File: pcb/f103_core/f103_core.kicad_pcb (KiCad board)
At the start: 2 copper layers, 29 parts, among them J1 Conn_02x20_Odd_Even, J4 Conn_01x04, J5 Conn_02x03_Odd_Even, SW1 SW_Push, U1 STM32F103C6Tx, U2 AMS1117-3.3, Y1 8M, Y2 32.768

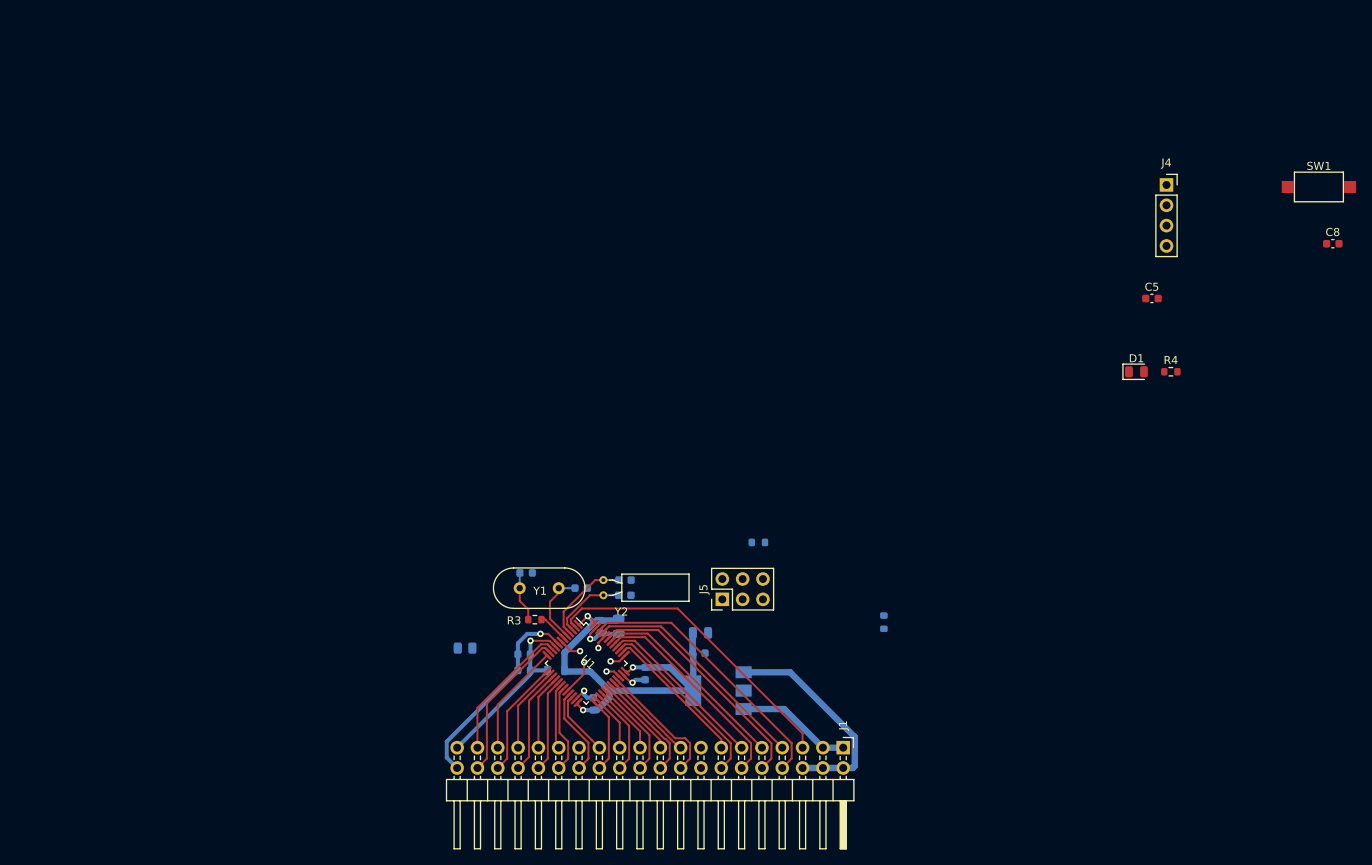
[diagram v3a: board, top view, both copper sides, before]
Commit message: Upadate pcb layout for f103_core board.
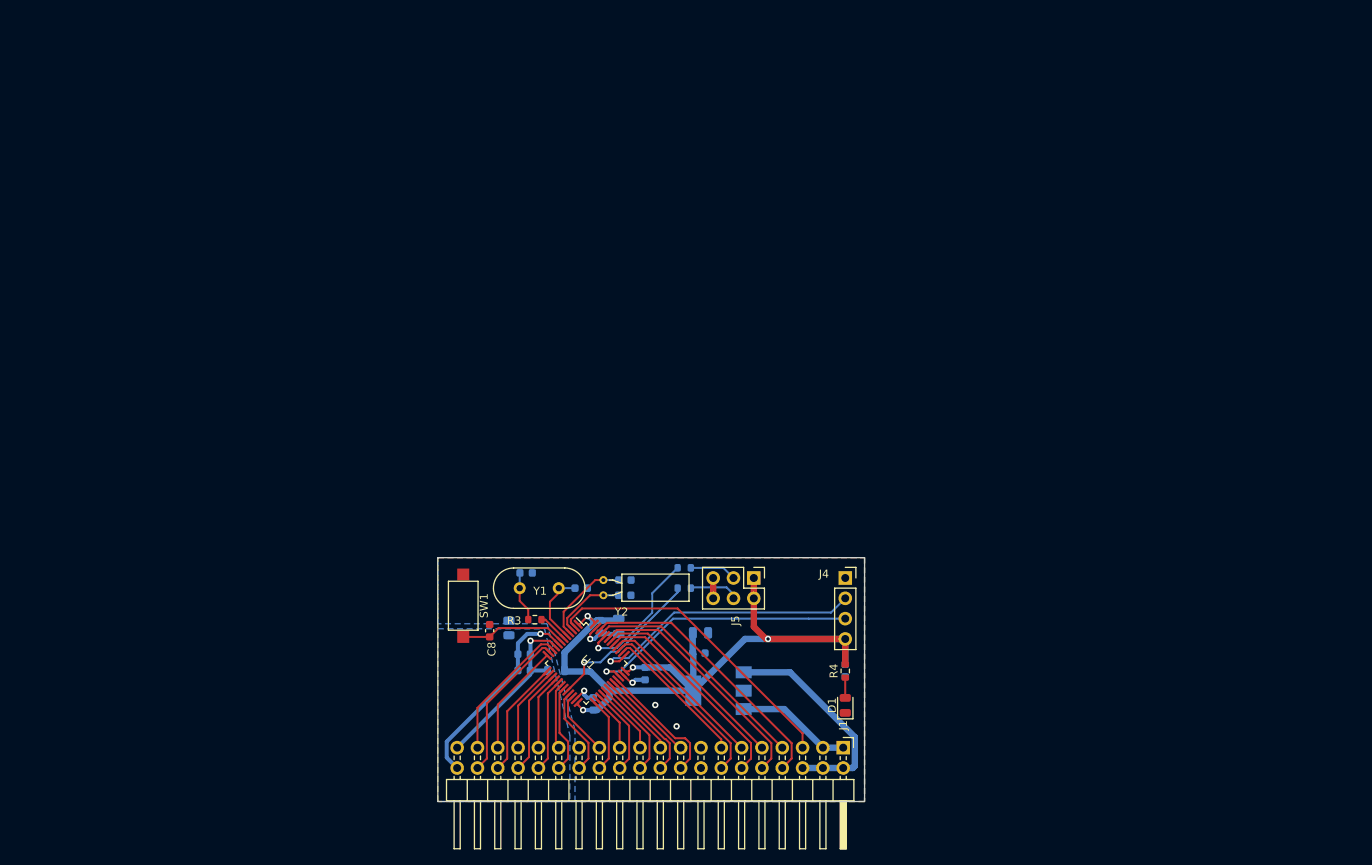
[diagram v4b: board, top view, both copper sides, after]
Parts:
- C5: moved to B.Cu
- moved SW1 119.1 mm to (106.7, 111.4), turned to 270 degrees
- moved C8 116.0 mm to (110.0, 114.5), turned to 90 degrees
- moved J4 63.5 mm to (154.4, 108.0)
- moved C5 60.3 mm to (154.4, 119.5), turned to 270 degrees
- moved D1 55.4 mm to (154.4, 123.9), turned to 90 degrees
- moved R4 55.3 mm to (154.4, 119.6), turned to 90 degrees
- moved R2 25.3 mm to (134.3, 109.2), turned to 0 degrees
- moved R1 9.80 mm to (134.3, 106.7)
- moved R5 6.03 mm to (112.4, 114.2), turned to 270 degrees
- moved J5 4.76 mm to (143.0, 108.0), turned to 270 degrees
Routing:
- net +3V3: track 56.1 -> 102.3 mm, vias 3 -> 4
- net /SYS_JTCK-SWCL: track 2.15 -> 34.7 mm
- net /SYS_JTMS-SWDIO: track 1.93 -> 34.5 mm
- net /BOOT1: track 4.49 -> 20.3 mm
- net /BOOT0: track 1.97 -> 17.5 mm
- net RESET: track 2.87 -> 13.4 mm, vias 1 -> 0
- net Net-(J5-Pad4): track 0.00 -> 6.34 mm
- net Net-(J5-Pad3): track 0.00 -> 5.97 mm
- net Net-(D1-Pad2): track 0.00 -> 2.54 mm
- net GND: track 40.0 -> 42.6 mm, vias 3 -> 5
- added copper zone on B.Cu, net GND
- added copper zone on F.Cu, net GND
- added copper zone on B.Cu, net GNDA
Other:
- board outline added: 53.3 x 30.5 mm

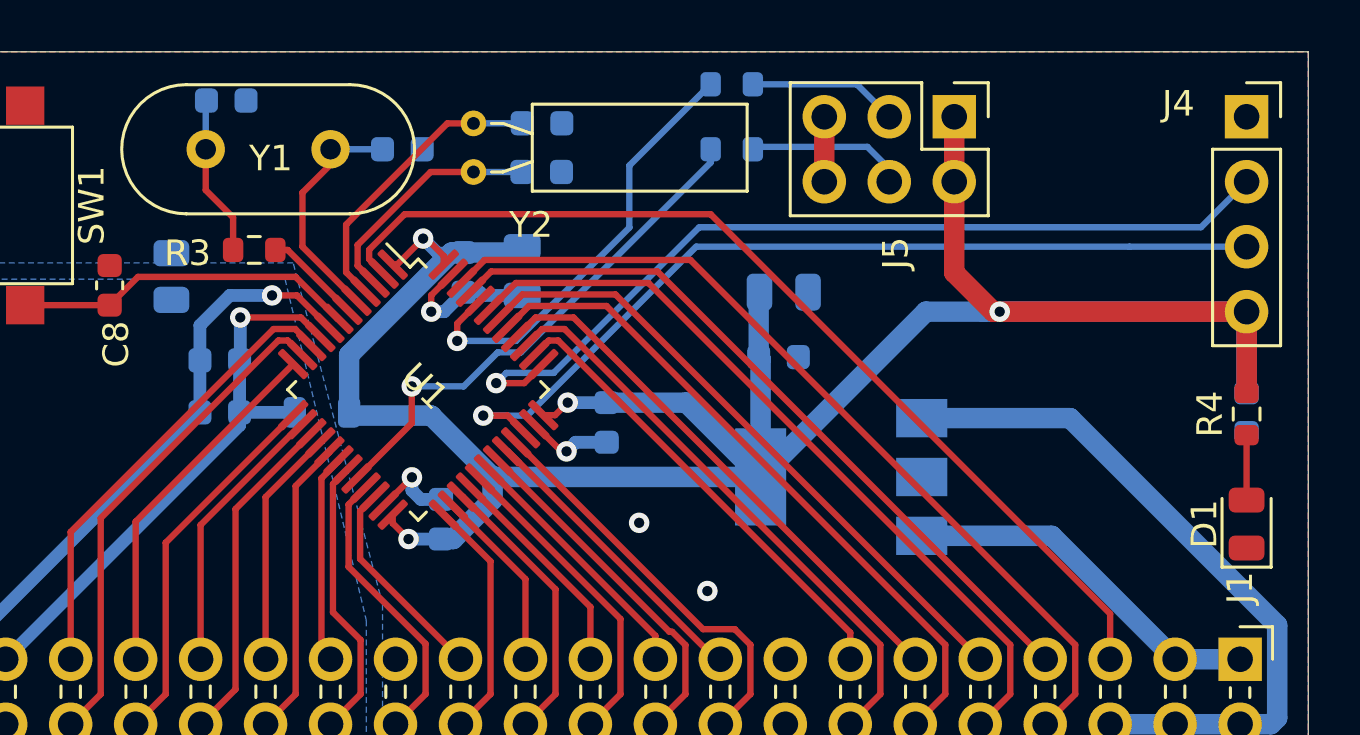
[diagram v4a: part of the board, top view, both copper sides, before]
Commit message: Add more ground vias for f103_core board.
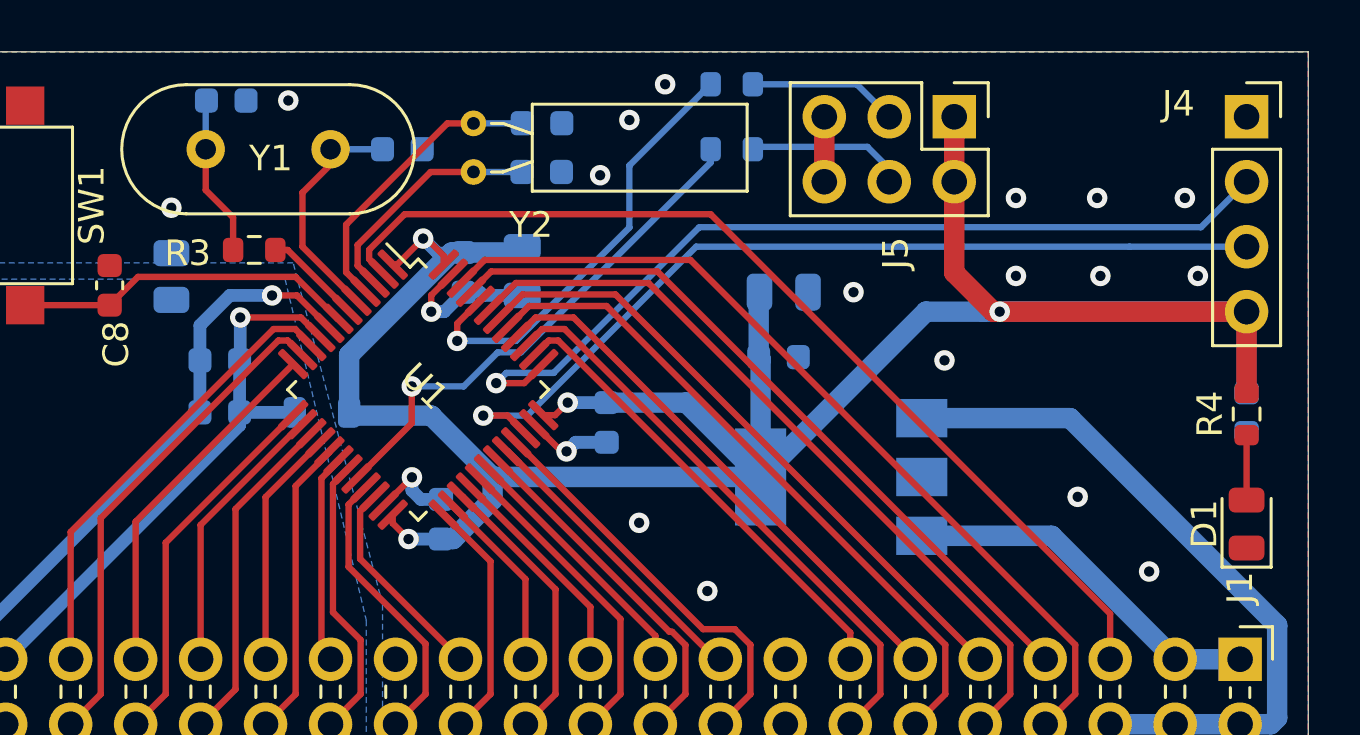
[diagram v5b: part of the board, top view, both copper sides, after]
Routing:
- net GND: vias 5 -> 20
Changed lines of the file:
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@@
-(kicad_pcb (version 20171130) (host pcbnew 5.1.10)
+(kicad_pcb (version 20171130) (host pcbnew 5.1.10-88a1d61d58~90~ubuntu20.04.1)
   (general
     (thickness 1.6)
     (drawings 4)
-    (tracks 290)
+    (tracks 305)
     (zones 0)
     (modules 29)
@@
       (effects (font (size 0.5 0.5) (thickness 0.08)) (justify mirror))
     )
-    (pad 2 smd roundrect (at 0.9125 0 270) (size 1.025 1.4) (layers B.Cu B.Paste B.Mask) (roundrect_rratio 0.243902)
+    (pad 2 smd roundrect (at 0.9125 0 270) (size 1.025 1.4) (layers B.Cu B.Paste B.Mask) (roundrect_rratio 0.2439014634146341)
       (net 17 GNDA))
-    (pad 1 smd roundrect (at -0.9125 0 270) (size 1.025 1.4) (layers B.Cu B.Paste B.Mask) (roundrect_rratio 0.243902)
+    (pad 1 smd roundrect (at -0.9125 0 270) (size 1.025 1.4) (layers B.Cu B.Paste B.Mask) (roundrect_rratio 0.2439014634146341)
       (net 2 GND))
     (model ${KISYS3DMOD}/Resistor_SMD.3dshapes/R_0805_2012Metric.wrl
@@
   (via (at 130.683 123.825) (size 0.8) (drill 0.4) (layers F.Cu B.Cu) (net 2))
   (via (at 133.35 126.492) (size 0.8) (drill 0.4) (layers F.Cu B.Cu) (net 2))
+  (via (at 116.967 107.315) (size 0.8) (drill 0.4) (layers F.Cu B.Cu) (net 2))
+  (via (at 131.699 106.68) (size 0.8) (drill 0.4) (layers F.Cu B.Cu) (net 2))
+  (via (at 130.302 108.077) (size 0.8) (drill 0.4) (layers F.Cu B.Cu) (net 2))
+  (via (at 129.159 110.236) (size 0.8) (drill 0.4) (layers F.Cu B.Cu) (net 2))
+  (via (at 145.415 111.125) (size 0.8) (drill 0.4) (layers F.Cu B.Cu) (net 2))
+  (via (at 148.59 111.125) (size 0.8) (drill 0.4) (layers F.Cu B.Cu) (net 2))
+  (via (at 152.019 111.125) (size 0.8) (drill 0.4) (layers F.Cu B.Cu) (net 2))
+  (via (at 139.065 114.808) (size 0.8) (drill 0.4) (layers F.Cu B.Cu) (net 2))
+  (via (at 145.415 114.173) (size 0.8) (drill 0.4) (layers F.Cu B.Cu) (net 2))
+  (via (at 148.717 114.173) (size 0.8) (drill 0.4) (layers F.Cu B.Cu) (net 2))
+  (via (at 152.527 114.173) (size 0.8) (drill 0.4) (layers F.Cu B.Cu) (net 2))
+  (via (at 142.621 117.475) (size 0.8) (drill 0.4) (layers F.Cu B.Cu) (net 2))
+  (via (at 147.828 122.809) (size 0.8) (drill 0.4) (layers F.Cu B.Cu) (net 2))
+  (via (at 150.622 125.73) (size 0.8) (drill 0.4) (layers F.Cu B.Cu) (net 2))
+  (via (at 112.395 111.506) (size 0.8) (drill 0.4) (layers F.Cu B.Cu) (net 2))
   (segment (start 114.809 113.157) (end 114.809 111.888) (width 0.25) (layer F.Cu) (net 3))
   (segment (start 113.738 110.817) (end 113.738 109.22) (width 0.25) (layer F.Cu) (net 3))
